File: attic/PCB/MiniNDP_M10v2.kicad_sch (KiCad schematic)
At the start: 14 parts, among them J1 Conn_02x20_Odd_Even, U1 AS6C8008_TSOPII, U2 HC238, U3 HC4040, U4 ABT841

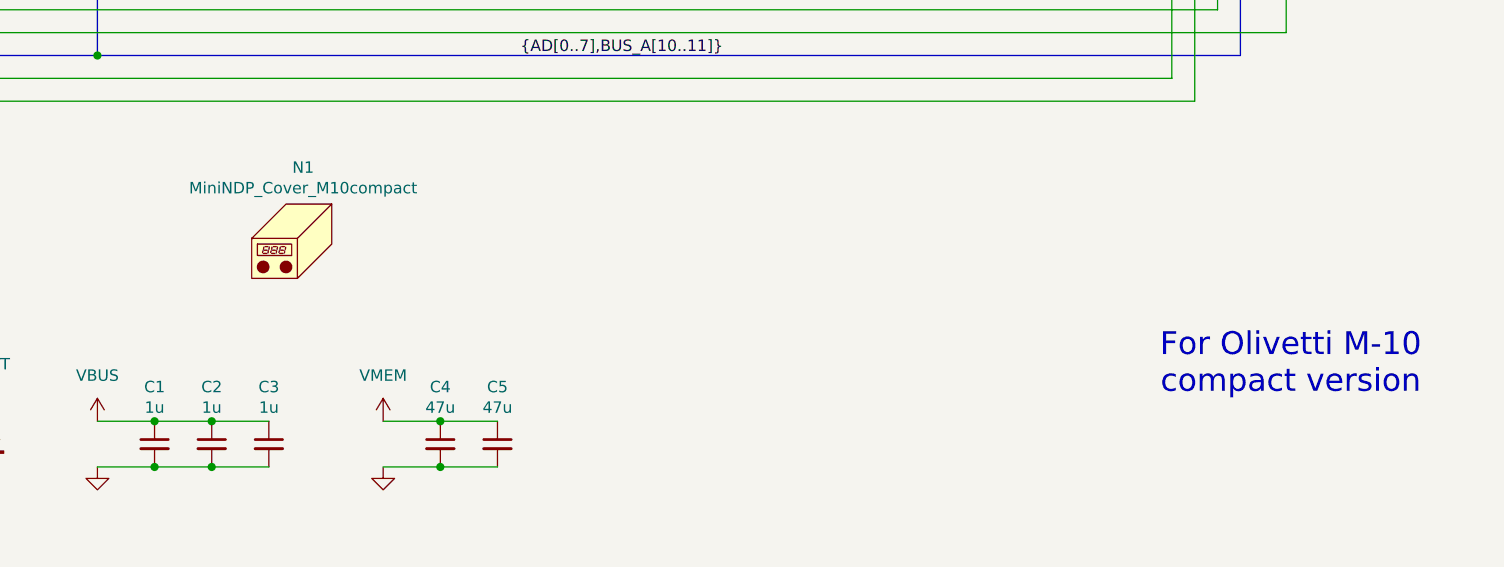
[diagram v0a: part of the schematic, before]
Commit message: M10 better layout, put old M10 versions in attic
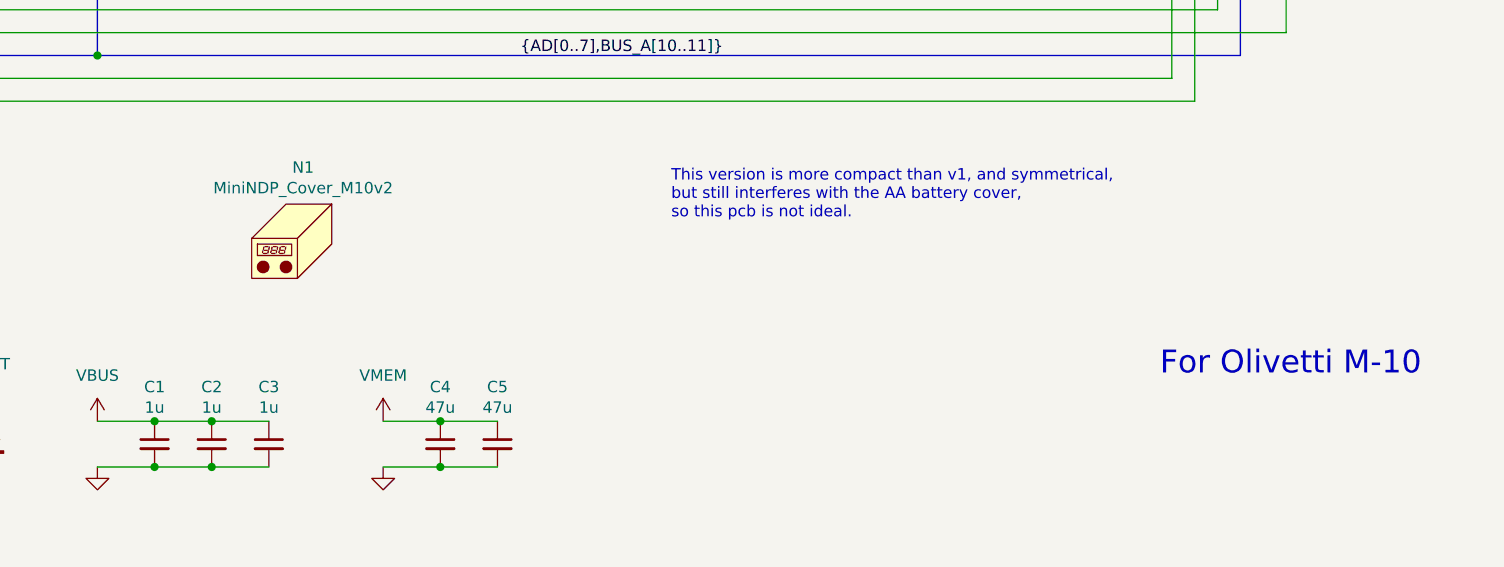
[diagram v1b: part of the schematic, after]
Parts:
- N1: value MiniNDP_Cover_M10compact -> MiniNDP_Cover_M10v2; footprint 000_LOCAL:MiniNDP_Cover_M10compact -> 000_LOCAL:MiniNDP_Cover_M10v2; MPN MiniNDP_Cover_M10compact.stl -> MiniNDP_Cover_M10v2.stl
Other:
- note added: "For Olivetti M-10"
- note added: "This version is more compact than v1, and symmetrical, but still interferes with the AA battery cover, so this pcb is not ideal."
- note removed: "For Olivetti M-10 compact version"
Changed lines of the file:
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@@
 		(comment 3 "Work-alike of NODE Systems DATAPAC / RAMPAC")
 	)
+	(text "This version is more compact than v1, and symmetrical,\nbut still interferes with the AA battery cover,\nso this pcb is not ideal."
+		(exclude_from_sim no)
+		(at 190.754 152.4 0)
+		(effects
+			(font
+				(size 1.27 1.27)
+			)
+			(justify left top)
+		)
+	)
 	(text "TANDY 102/200\nSYSTEM BUS"
 		(exclude_from_sim no)
@@
 		)
 	)
-	(text "For Olivetti M-10\ncompact version"
+	(text "For Olivetti M-10"
 		(exclude_from_sim no)
 		(at 259.588 173.99 0)
@@
 		)
 		(instances
-			(project "MiniNDP_M10c"
+			(project "MiniNDP_M10v2"
 				(path "/f15c2929-5cf4-4b4e-965d-148e1bec8a42"
 					(reference "U1")
@@
 		)
 		(instances
-			(project "MiniNDP_M10c"
+			(project "MiniNDP_M10v2"
 				(path "/f15c2929-5cf4-4b4e-965d-148e1bec8a42"
 					(reference "#PWR08")
@@
 		)
 		(instances
-			(project "MiniNDP_M10c"
+			(project "MiniNDP_M10v2"
 				(path "/f15c2929-5cf4-4b4e-965d-148e1bec8a42"
 					(reference "U2")
@@
 		)
 		(instances
-			(project "MiniNDP_M10c"
+			(project "MiniNDP_M10v2"
 				(path "/f15c2929-5cf4-4b4e-965d-148e1bec8a42"
 					(reference "#PWR010")
@@
 		)
 		(instances
-			(project "MiniNDP_M10c"
+			(project "MiniNDP_M10v2"
 				(path "/f15c2929-5cf4-4b4e-965d-148e1bec8a42"
 					(reference "#PWR01")
@@
 		)
 		(instances
-			(project "MiniNDP_M10c"
+			(project "MiniNDP_M10v2"
 				(path "/f15c2929-5cf4-4b4e-965d-148e1bec8a42"
 					(reference "BT1")
@@
 		)
 		(instances
-			(project "MiniNDP_M10c"
+			(project "MiniNDP_M10v2"
 				(path "/f15c2929-5cf4-4b4e-965d-148e1bec8a42"
 					(reference "#PWR022")
@@
 		)
 		(instances
-			(project "MiniNDP_M10c"
+			(project "MiniNDP_M10v2"
 				(path "/f15c2929-5cf4-4b4e-965d-148e1bec8a42"
 					(reference "#PWR05")
@@
 		)
 		(instances
-			(project "MiniNDP_M10c"
+			(project "MiniNDP_M10v2"
 				(path "/f15c2929-5cf4-4b4e-965d-148e1bec8a42"
 					(reference "#PWR012")
@@
 		)
 		(instances
-			(project "MiniNDP_M10c"
+			(project "MiniNDP_M10v2"
 				(path "/f15c2929-5cf4-4b4e-965d-148e1bec8a42"
 					(reference "#FLG01")
@@
 		)
 		(instances
-			(project "MiniNDP_M10c"
+			(project "MiniNDP_M10v2"
 				(path "/f15c2929-5cf4-4b4e-965d-148e1bec8a42"
 					(reference "#PWR058")
@@
 		)
 		(instances
-			(project "MiniNDP_M10c"
+			(project "MiniNDP_M10v2"
 				(path "/f15c2929-5cf4-4b4e-965d-148e1bec8a42"
 					(reference "#PWR019")
@@
 		)
 		(instances
-			(project "MiniNDP_M10c"
+			(project "MiniNDP_M10v2"
 				(path "/f15c2929-5cf4-4b4e-965d-148e1bec8a42"
 					(reference "#PWR07")
@@
 		)
 		(instances
-			(project "MiniNDP_M10c"
+			(project "MiniNDP_M10v2"
 				(path "/f15c2929-5cf4-4b4e-965d-148e1bec8a42"
 					(reference "#PWR042")
@@
 		)
 		(instances
-			(project "MiniNDP_M10c"
+			(project "MiniNDP_M10v2"
 				(path "/f15c2929-5cf4-4b4e-965d-148e1bec8a42"
 					(reference "#PWR057")
@@
 		)
 		(instances
-			(project "MiniNDP_M10c"
+			(project "MiniNDP_M10v2"
 				(path "/f15c2929-5cf4-4b4e-965d-148e1bec8a42"
 					(reference "#PWR03")
@@
 		)
 		(instances
-			(project "MiniNDP_M10c"
+			(project "MiniNDP_M10v2"
 				(path "/f15c2929-5cf4-4b4e-965d-148e1bec8a42"
 					(reference "#PWR055")
@@
 		)
 		(instances
-			(project "MiniNDP_M10c"
+			(project "MiniNDP_M10v2"
 				(path "/f15c2929-5cf4-4b4e-965d-148e1bec8a42"
 					(reference "DA1")
@@
 			)
 		)
-		(property "Value" "MiniNDP_Cover_M10compact"
+		(property "Value" "MiniNDP_Cover_M10v2"
 			(at 149.86 154.432 0)
 			(effects
@@
 			)
 		)
-		(property "Footprint" "000_LOCAL:MiniNDP_Cover_M10compact"
+		(property "Footprint" "000_LOCAL:MiniNDP_Cover_M10v2"
 			(at 151.13 158.75 0)
 			(effects
@@
 			)
 		)
-		(property "Description" "Snap cover for MiniNDP M10c compact version"
+		(property "Description" "Snap cover for MiniNDP M10v2"
 			(at 149.86 160.02 0)
 			(effects
@@
 			)
 		)
-		(property "MPN" "MiniNDP_Cover_M10compact.stl"
+		(property "MPN" "MiniNDP_Cover_M10v2.stl"
 			(at 149.86 160.02 0)
 			(effects
@@
 		)
 		(instances
-			(project "MiniNDP_M10c"
+			(project "MiniNDP_M10v2"
 				(path "/f15c2929-5cf4-4b4e-965d-148e1bec8a42"
 					(reference "N1")
@@
 		)
 		(instances
-			(project "MiniNDP_M10c"
+			(project "MiniNDP_M10v2"
 				(path "/f15c2929-5cf4-4b4e-965d-148e1bec8a42"
 					(reference "C5")
@@
 		)
 		(instances
-			(project "MiniNDP_M10c"
+			(project "MiniNDP_M10v2"
 				(path "/f15c2929-5cf4-4b4e-965d-148e1bec8a42"
 					(reference "C2")
@@
 		)
 		(instances
-			(project "MiniNDP_M10c"
+			(project "MiniNDP_M10v2"
 				(path "/f15c2929-5cf4-4b4e-965d-148e1bec8a42"
 					(reference "#FLG03")
@@
 		)
 		(instances
-			(project "MiniNDP_M10c"
+			(project "MiniNDP_M10v2"
 				(path "/f15c2929-5cf4-4b4e-965d-148e1bec8a42"
 					(reference "#PWR023")
@@
 		)
 		(instances
-			(project "MiniNDP_M10c"
+			(project "MiniNDP_M10v2"
 				(path "/f15c2929-5cf4-4b4e-965d-148e1bec8a42"
 					(reference "#PWR06")
@@
 		)
 		(instances
-			(project "MiniNDP_M10c"
+			(project "MiniNDP_M10v2"
 				(path "/f15c2929-5cf4-4b4e-965d-148e1bec8a42"
 					(reference "U3")
@@
 		)
 		(instances
-			(project "MiniNDP_M10c"
+			(project "MiniNDP_M10v2"
 				(path "/f15c2929-5cf4-4b4e-965d-148e1bec8a42"
 					(reference "#PWR027")
@@
 		)
 		(instances
-			(project "MiniNDP_M10c"
+			(project "MiniNDP_M10v2"
 				(path "/f15c2929-5cf4-4b4e-965d-148e1bec8a42"
 					(reference "#PWR014")
@@
 		)
 		(instances
-			(project "MiniNDP_M10c"
+			(project "MiniNDP_M10v2"
 				(path "/f15c2929-5cf4-4b4e-965d-148e1bec8a42"
 					(reference "R1")
@@
 		)
 		(instances
-			(project "MiniNDP_M10c"
+			(project "MiniNDP_M10v2"
 				(path "/f15c2929-5cf4-4b4e-965d-148e1bec8a42"
 					(reference "#PWR04")
@@
 		)
 		(instances
-			(project "MiniNDP_M10c"
+			(project "MiniNDP_M10v2"
 				(path "/f15c2929-5cf4-4b4e-965d-148e1bec8a42"
 					(reference "#FLG02")
@@
 		)
 		(instances
-			(project "MiniNDP_M10c"
+			(project "MiniNDP_M10v2"
 				(path "/f15c2929-5cf4-4b4e-965d-148e1bec8a42"
 					(reference "#PWR09")
@@
 		)
 		(instances
-			(project "MiniNDP_M10c"
+			(project "MiniNDP_M10v2"
 				(path "/f15c2929-5cf4-4b4e-965d-148e1bec8a42"
 					(reference "C4")
@@
 		)
 		(instances
-			(project "MiniNDP_M10c"
+			(project "MiniNDP_M10v2"
 				(path "/f15c2929-5cf4-4b4e-965d-148e1bec8a42"
 					(reference "#PWR025")
@@
 		)
 		(instances
-			(project "MiniNDP_M10c"
+			(project "MiniNDP_M10v2"
 				(path "/f15c2929-5cf4-4b4e-965d-148e1bec8a42"
 					(reference "J1")
@@
 		)
 		(instances
-			(project "MiniNDP_M10c"
+			(project "MiniNDP_M10v2"
 				(path "/f15c2929-5cf4-4b4e-965d-148e1bec8a42"
 					(reference "#PWR041")
@@
 		)
 		(instances
-			(project "MiniNDP_M10c"
+			(project "MiniNDP_M10v2"
 				(path "/f15c2929-5cf4-4b4e-965d-148e1bec8a42"
 					(reference "C3")
@@
 		)
 		(instances
-			(project "MiniNDP_M10c"
+			(project "MiniNDP_M10v2"
 				(path "/f15c2929-5cf4-4b4e-965d-148e1bec8a42"
 					(reference "#PWR032")
@@
 		)
 		(instances
-			(project "MiniNDP_M10c"
+			(project "MiniNDP_M10v2"
 				(path "/f15c2929-5cf4-4b4e-965d-148e1bec8a42"
 					(reference "U4")
@@
 		)
 		(instances
-			(project "MiniNDP_M10c"
+			(project "MiniNDP_M10v2"
 				(path "/f15c2929-5cf4-4b4e-965d-148e1bec8a42"
 					(reference "#PWR033")
@@
 		)
 		(instances
-			(project "MiniNDP_M10c"
+			(project "MiniNDP_M10v2"
 				(path "/f15c2929-5cf4-4b4e-965d-148e1bec8a42"
 					(reference "#PWR011")
@@
 		)
 		(instances
-			(project "MiniNDP_M10c"
+			(project "MiniNDP_M10v2"
 				(path "/f15c2929-5cf4-4b4e-965d-148e1bec8a42"
 					(reference "C1")
@@
 		)
 		(instances
-			(project "MiniNDP_M10c"
+			(project "MiniNDP_M10v2"
 				(path "/f15c2929-5cf4-4b4e-965d-148e1bec8a42"
 					(reference "#PWR016")
